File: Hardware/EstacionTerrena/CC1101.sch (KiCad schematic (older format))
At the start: 1 part, among them U3 CC1101

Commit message: Esquema de estación terrena casi terminado. falta revision.
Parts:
- added C10, C9: 15pF, symbol Device:C_Small
- added C11, C12, C13, C14, C6, C7, C8: 100nF, symbol Device:C_Small
- added C15, C16: n.a, symbol Device:C_Small
- added L1: 12nH, symbol Device:L
- added R4: 56k, symbol Device:R
- added R5, R6: 0R, symbol Device:R
- added U5: 0915BM15A0001, symbol AXTEC_IC:0915BM15A0001
- added Y2: 26MHz, symbol Device:Crystal_GND2
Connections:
- net labels added: RF_N, RF_P
- wire segments 20 -> 80

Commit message: Asignados footprints a esquema de estación terrena
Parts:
- removed U5: 0915BM15A0001, symbol AXTEC_IC:0915BM15A0001
- removed Y2: 26MHz, symbol Device:Crystal_GND2
- added U5: 0915BM15A0001E, 0915BM15A0001E, symbol SamacSys_Parts:0915BM15A0001E
- added Y2: 26 MHz, Crystal:Crystal_SMD_2520-4Pin_2.5x2.0mm, symbol Device:Crystal_GND24
- C10, C9: value 15pF -> 18pF; footprint (none) -> Capacitor_SMD:C_0603_1608Metric; Dielectric (none) -> NP0; Manufacturer Part Number (none) -> VJ0603A180KXQPW1BC; Voltage (none) -> 10V
- C11, C12, C13, C14, C6, C7, C8: footprint (none) -> Capacitor_SMD:C_0603_1608Metric; Dielectric (none) -> X7R; Manufacturer Part Number (none) -> EMK107B7104KAHT; Voltage (none) -> 16V
- C15, C16: footprint (none) -> Capacitor_SMD:C_0402_1005Metric
- L1: footprint (none) -> Inductor_SMD:L_0402_1005Metric; Manufacturer Part Number (none) -> L-07C12NJV6
- R5, R6: footprint (none) -> Resistor_SMD:R_0402_1005Metric; Manufacturer Part Number (none) -> RC0402JR-070RL
- renumbered U3 to U4
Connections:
- wire segments 80 -> 79
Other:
- moved on the sheet: C15, C16, L1, R5

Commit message: PCB inicial para estación terrena
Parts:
- removed U4: CC1101, symbol AXTEC_IC:CC1101
- added U4: CC1101RGP, QFN50P400X400X100-21N-D, symbol SamacSys_Parts:CC1101RGP
- R4: footprint (none) -> Resistor_SMD:R_0603_1608Metric_Pad1.05x0.95mm_HandSolder
- renumbered C13 to C12, C12 to C13
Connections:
- wire segments 79 -> 80
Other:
- moved on the sheet: C10, C11, C12, C13, C14, C15, C16, C6, C7, C8, C9, L1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

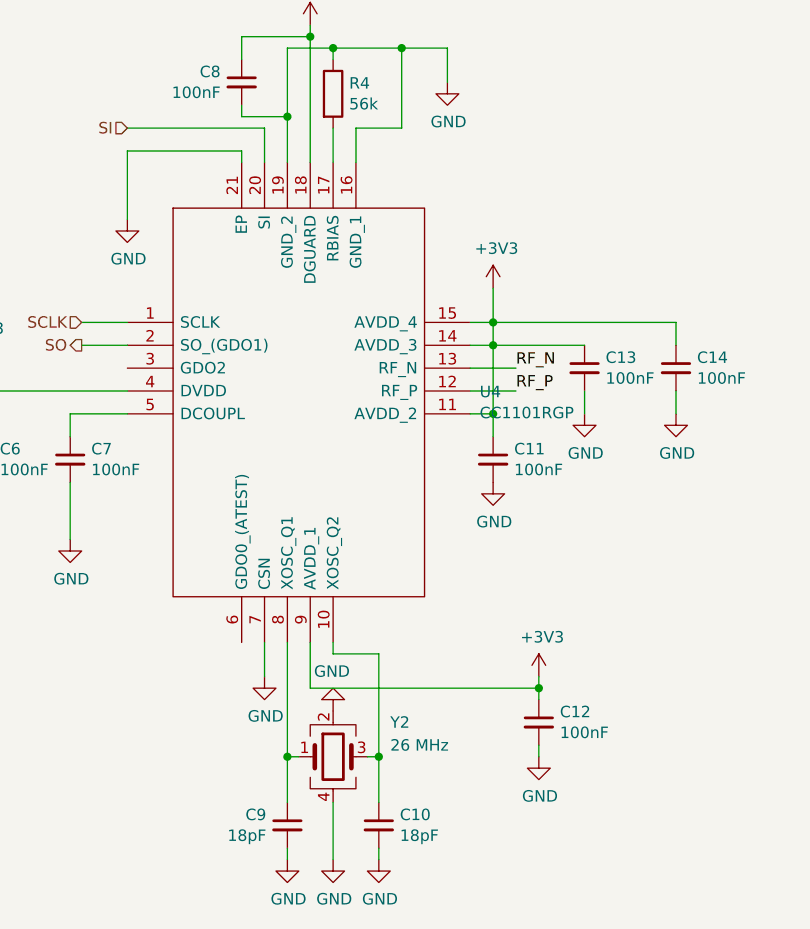
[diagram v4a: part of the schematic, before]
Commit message: Numeros de parte para estación terrena. Capacitores de 15pF para cristal de CC1101 (en lugar de 18pF).
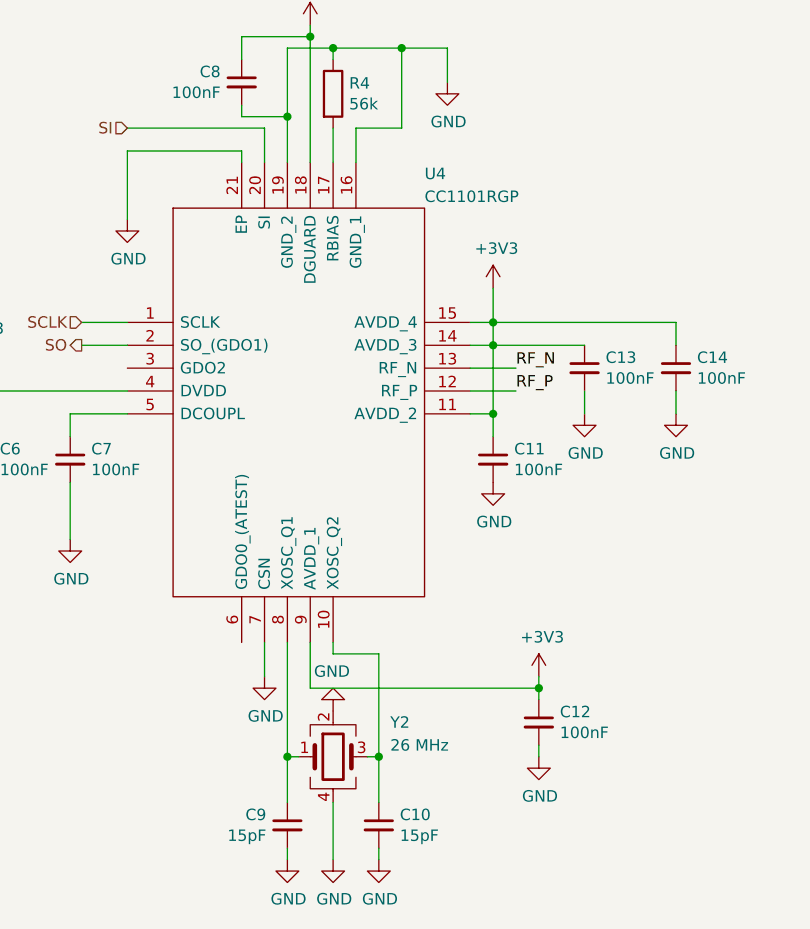
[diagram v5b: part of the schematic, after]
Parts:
- C10, C9: value 18pF -> 15pF; Manufacturer Part Number VJ0603A180KXQPW1BC -> VJ0603A150KXJPW1BC
- R4: Manufacturer Part Number (none) -> RC0402FR-0756KL
- U4: Manufacturer Part Number (none) -> CC1101RGP; Manufacturer_Part_Number CC1101RGP -> (none)
- U5: Manufacturer Part Number (none) -> 0915BM15A0001E; Manufacturer_Part_Number 0915BM15A0001E -> (none)
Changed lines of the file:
@@
 F 2 "Resistor_SMD:R_0603_1608Metric_Pad1.05x0.95mm_HandSolder" V 3730 2150 50  0001 C CNN
 F 3 "~" H 3800 2150 50  0001 C CNN
+F 4 "RC0402FR-0756KL" H 3800 2150 50  0001 C CNN "Manufacturer Part Number"
 	1    3800 2150
 	1    0    0    -1
@@
 AR Path="/5B9A8077/5BF04031" Ref="C9"  Part="1"
 F 0 "C9" H 3692 5396 50  0000 L CNN
-F 1 "18pF" H 3692 5305 50  0000 L CNN
+F 1 "15pF" H 3692 5305 50  0000 L CNN
 F 2 "Capacitor_SMD:C_0603_1608Metric" H 3600 5350 50  0001 C CNN
 F 3 "~" H 3600 5350 50  0001 C CNN
 F 4 "NP0" H 3600 5350 50  0001 C CNN "Dielectric"
 F 5 "10V" H 3600 5350 50  0001 C CNN "Voltage"
-F 6 "VJ0603A180KXQPW1BC" H 3600 5350 50  0001 C CNN "Manufacturer Part Number"
+F 6 "VJ0603A150KXJPW1BC" H 3600 5350 50  0001 C CNN "Manufacturer Part Number"
 	1    3600 5350
 	-1   0    0    -1
@@
 AR Path="/5B9A8077/5BF0725F" Ref="C10"  Part="1"
 F 0 "C10" H 4092 5396 50  0000 L CNN
-F 1 "18pF" H 4092 5305 50  0000 L CNN
+F 1 "15pF" H 4092 5305 50  0000 L CNN
 F 2 "Capacitor_SMD:C_0603_1608Metric" H 4000 5350 50  0001 C CNN
 F 3 "~" H 4000 5350 50  0001 C CNN
 F 4 "NP0" H 4000 5350 50  0001 C CNN "Dielectric"
 F 5 "10V" H 4000 5350 50  0001 C CNN "Voltage"
-F 6 "VJ0603A180KXQPW1BC" H 4000 5350 50  0001 C CNN "Manufacturer Part Number"
+F 6 "VJ0603A150KXJPW1BC" H 4000 5350 50  0001 C CNN "Manufacturer Part Number"
 	1    4000 5350
 	1    0    0    -1
@@
 F 5 "0.8" H 7500 3300 50  0001 L CNN "Height"
 F 6 "JOHANSON TECHNOLOGY" H 7500 3200 50  0001 L CNN "Manufacturer_Name"
-F 7 "0915BM15A0001E" H 7500 3100 50  0001 L CNN "Manufacturer_Part_Number"
+F 7 "0915BM15A0001E" H 7500 3100 50  0001 L CNN "Manufacturer Part Number"
 F 8 "0915BM15A0001E" H 7500 3000 50  0001 L CNN "Arrow Part Number"
 	1    7150 3400
@@
 U 1 1 5BBFFFB0
 P 2900 3150
-F 0 "U4" H 4441 2846 50  0000 L CNN
-F 1 "CC1101RGP" H 4441 2754 50  0000 L CNN
+F 0 "U4" H 4200 3800 50  0000 L CNN
+F 1 "CC1101RGP" H 4200 3700 50  0000 L CNN
 F 2 "QFN50P400X400X100-21N-D" H 4250 3650 50  0001 L CNN
 F 3 "http://www.ti.com/lit/ds/symlink/cc1101.pdf" H 4250 3550 50  0001 L CNN
@@
 F 5 "1" H 4250 3350 50  0001 L CNN "Height"
 F 6 "Texas Instruments" H 4250 3250 50  0001 L CNN "Manufacturer_Name"
-F 7 "CC1101RGP" H 4250 3150 50  0001 L CNN "Manufacturer_Part_Number"
+F 7 "CC1101RGP" H 4250 3150 50  0001 L CNN "Manufacturer Part Number"
 F 8 "8203068P" H 4250 3050 50  0001 L CNN "RS Part Number"
 F 9 "http://uk.rs-online.com/web/p/products/8203068P" H 4250 2950 50  0001 L CNN "RS Price/Stock"

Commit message: Agregado jumper para CS en estacion terrena
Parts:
- U4: footprint QFN50P400X400X100-21N-D -> SamacSys_Parts:QFN50P400X400X100-21N-D
- U5: footprint 0915BM15A0001E -> SamacSys_Parts:0915BM15A0001E
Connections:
- net GND: no longer U4.7 (CSN)
- new net CS: U4.7 (CSN)
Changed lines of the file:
@@
 Text HLabel 2900 2300 0    50   Input ~ 0
 SI
-$Comp
-L power:GND #PWR026
-U 1 1 5B9A819D
-P 3500 4700
-F 0 "#PWR026" H 3500 4450 50  0001 C CNN
-F 1 "GND" H 3505 4527 50  0000 C CNN
-F 2 "" H 3500 4700 50  0001 C CNN
-F 3 "" H 3500 4700 50  0001 C CNN
-	1    3500 4700
-	1    0    0    -1
-$EndComp
-Wire Wire Line
-	3500 4700 3500 4550
 Text HLabel 9400 3500 2    50   BiDi ~ 0
 ANT
@@
 F 0 "U5" H 7150 3766 50  0000 C CNN
 F 1 "0915BM15A0001E" H 7150 3674 50  0000 C CNN
-F 2 "0915BM15A0001E" H 7500 3600 50  0001 L CNN
+F 2 "SamacSys_Parts:0915BM15A0001E" H 7500 3600 50  0001 L CNN
 F 3 "http://www.mouser.com/datasheet/2/611/0915BM15A0001-242333.pdf" H 7500 3500 50  0001 L CNN
 F 4 "Signal Conditioning 915MHz BALUN/FILTER" H 7500 3400 50  0001 L CNN "Description"
@@
 F 0 "U4" H 4200 3800 50  0000 L CNN
 F 1 "CC1101RGP" H 4200 3700 50  0000 L CNN
-F 2 "QFN50P400X400X100-21N-D" H 4250 3650 50  0001 L CNN
+F 2 "SamacSys_Parts:QFN50P400X400X100-21N-D" H 4250 3650 50  0001 L CNN
 F 3 "http://www.ti.com/lit/ds/symlink/cc1101.pdf" H 4250 3550 50  0001 L CNN
 F 4 "Texas Instruments CC1101RGP, RF Transceiver IC Triple Band 1.8  3.6 V 20-Pin QFN" H 4250 3450 50  0001 L CNN "Description"
@@
 	1    0    0    -1
 $EndComp
+Text HLabel 3150 4700 0    50   Input ~ 0
+CS
+Wire Wire Line
+	3150 4700 3500 4700
+Wire Wire Line
+	3500 4700 3500 4550
 $EndSCHEMATC

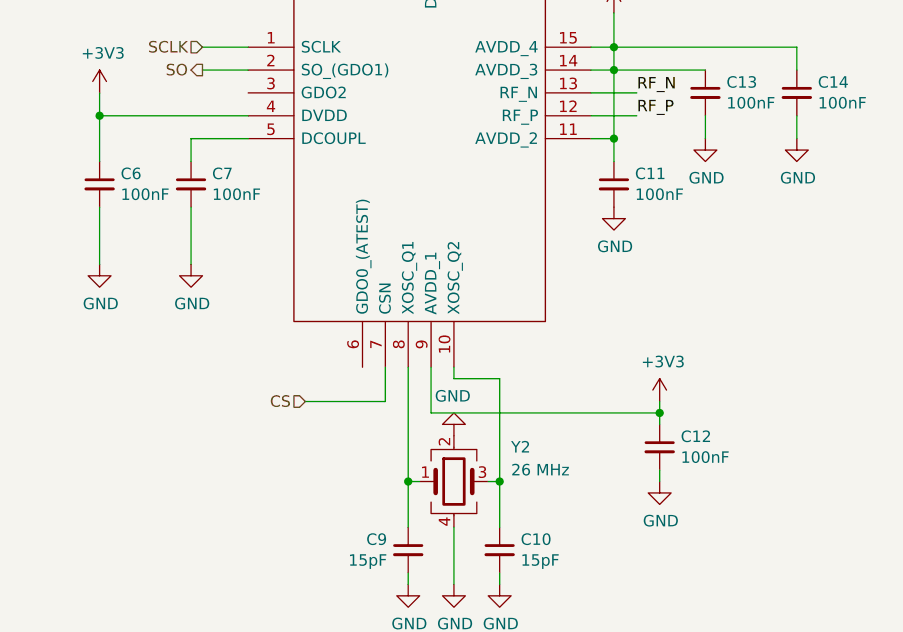
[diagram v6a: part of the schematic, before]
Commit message: Componentes 0402 para el CC1101 en estación terrena
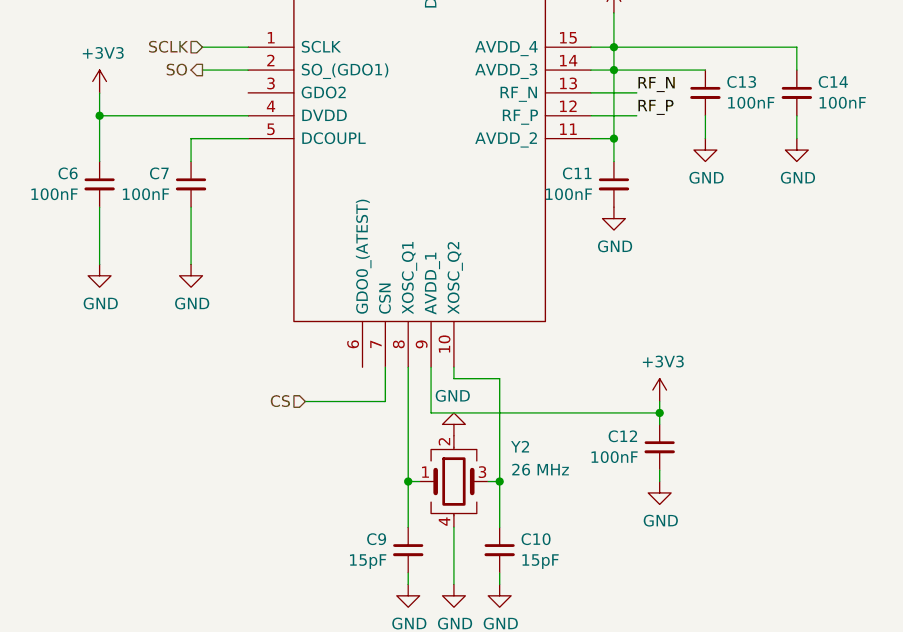
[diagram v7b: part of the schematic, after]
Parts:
- C10, C9: footprint Capacitor_SMD:C_0603_1608Metric -> Capacitor_SMD:C_0402_1005Metric; Manufacturer Part Number VJ0603A150KXJPW1BC -> C0402C150J5GACTU
- C11, C12, C13, C14, C6, C7, C8: footprint Capacitor_SMD:C_0603_1608Metric -> Capacitor_SMD:C_0402_1005Metric; Manufacturer Part Number EMK107B7104KAHT -> GCM155R71C104KA55D
- R4: footprint Resistor_SMD:R_0603_1608Metric_Pad1.05x0.95mm_HandSolder -> Resistor_SMD:R_0402_1005Metric
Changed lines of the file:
@@
 F 0 "R4" H 3870 2196 50  0000 L CNN
 F 1 "56k" H 3870 2105 50  0000 L CNN
-F 2 "Resistor_SMD:R_0603_1608Metric_Pad1.05x0.95mm_HandSolder" V 3730 2150 50  0001 C CNN
+F 2 "Resistor_SMD:R_0402_1005Metric" V 3730 2150 50  0001 C CNN
 F 3 "~" H 3800 2150 50  0001 C CNN
 F 4 "RC0402FR-0756KL" H 3800 2150 50  0001 C CNN "Manufacturer Part Number"
@@
 F 0 "C8" H 3492 2146 50  0000 L CNN
 F 1 "100nF" H 3492 2055 50  0000 L CNN
-F 2 "Capacitor_SMD:C_0603_1608Metric" H 3400 2100 50  0001 C CNN
+F 2 "Capacitor_SMD:C_0402_1005Metric" H 3400 2100 50  0001 C CNN
 F 3 "~" H 3400 2100 50  0001 C CNN
 F 4 "X7R" H 3400 2100 50  0001 C CNN "Dielectric"
 F 5 "16V" H 3400 2100 50  0001 C CNN "Voltage"
-F 6 "EMK107B7104KAHT" H 3400 2100 50  0001 C CNN "Manufacturer Part Number"
+F 6 "GCM155R71C104KA55D" H 3400 2100 50  0001 C CNN "Manufacturer Part Number"
 	1    3400 2100
 	-1   0    0    -1
-$EndComp
-$Comp
-L Device:C_Small C?
-U 1 1 5BEFB6E8
-P 2250 3750
-AR Path="/5B9997DB/5BEFB6E8" Ref="C?"  Part="1"
-AR Path="/5B9A8077/5BEFB6E8" Ref="C6"  Part="1"
-F 0 "C6" H 2342 3796 50  0000 L CNN
-F 1 "100nF" H 2342 3705 50  0000 L CNN
-F 2 "Capacitor_SMD:C_0603_1608Metric" H 2250 3750 50  0001 C CNN
-F 3 "~" H 2250 3750 50  0001 C CNN
-F 4 "X7R" H 2250 3750 50  0001 C CNN "Dielectric"
-F 5 "16V" H 2250 3750 50  0001 C CNN "Voltage"
-F 6 "EMK107B7104KAHT" H 2250 3750 50  0001 C CNN "Manufacturer Part Number"
-	1    2250 3750
-	1    0    0    -1
-$EndComp
-$Comp
-L Device:C_Small C?
-U 1 1 5BEFB74F
-P 2650 3750
-AR Path="/5B9997DB/5BEFB74F" Ref="C?"  Part="1"
-AR Path="/5B9A8077/5BEFB74F" Ref="C7"  Part="1"
-F 0 "C7" H 2742 3796 50  0000 L CNN
-F 1 "100nF" H 2742 3705 50  0000 L CNN
-F 2 "Capacitor_SMD:C_0603_1608Metric" H 2650 3750 50  0001 C CNN
-F 3 "~" H 2650 3750 50  0001 C CNN
-F 4 "X7R" H 2650 3750 50  0001 C CNN "Dielectric"
-F 5 "16V" H 2650 3750 50  0001 C CNN "Voltage"
-F 6 "EMK107B7104KAHT" H 2650 3750 50  0001 C CNN "Manufacturer Part Number"
-	1    2650 3750
-	1    0    0    -1
-$EndComp
-$Comp
-L Device:C_Small C?
-U 1 1 5BEFB898
-P 4700 4900
-AR Path="/5B9997DB/5BEFB898" Ref="C?"  Part="1"
-AR Path="/5B9A8077/5BEFB898" Ref="C12"  Part="1"
-F 0 "C12" H 4792 4946 50  0000 L CNN
-F 1 "100nF" H 4792 4855 50  0000 L CNN
-F 2 "Capacitor_SMD:C_0603_1608Metric" H 4700 4900 50  0001 C CNN
-F 3 "~" H 4700 4900 50  0001 C CNN
-F 4 "X7R" H 4700 4900 50  0001 C CNN "Dielectric"
-F 5 "16V" H 4700 4900 50  0001 C CNN "Voltage"
-F 6 "EMK107B7104KAHT" H 4700 4900 50  0001 C CNN "Manufacturer Part Number"
-	1    4700 4900
-	1    0    0    -1
-$EndComp
-$Comp
-L Device:C_Small C?
-U 1 1 5BEFBAA8
-P 4500 3750
-AR Path="/5B9997DB/5BEFBAA8" Ref="C?"  Part="1"
-AR Path="/5B9A8077/5BEFBAA8" Ref="C11"  Part="1"
-F 0 "C11" H 4592 3796 50  0000 L CNN
-F 1 "100nF" H 4592 3705 50  0000 L CNN
-F 2 "Capacitor_SMD:C_0603_1608Metric" H 4500 3750 50  0001 C CNN
-F 3 "~" H 4500 3750 50  0001 C CNN
-F 4 "X7R" H 4500 3750 50  0001 C CNN "Dielectric"
-F 5 "16V" H 4500 3750 50  0001 C CNN "Voltage"
-F 6 "EMK107B7104KAHT" H 4500 3750 50  0001 C CNN "Manufacturer Part Number"
-	1    4500 3750
-	1    0    0    -1
-$EndComp
-$Comp
-L Device:C_Small C?
-U 1 1 5BEFBAF0
-P 4900 3350
-AR Path="/5B9997DB/5BEFBAF0" Ref="C?"  Part="1"
-AR Path="/5B9A8077/5BEFBAF0" Ref="C13"  Part="1"
-F 0 "C13" H 4992 3396 50  0000 L CNN
-F 1 "100nF" H 4992 3305 50  0000 L CNN
-F 2 "Capacitor_SMD:C_0603_1608Metric" H 4900 3350 50  0001 C CNN
-F 3 "~" H 4900 3350 50  0001 C CNN
-F 4 "X7R" H 4900 3350 50  0001 C CNN "Dielectric"
-F 5 "16V" H 4900 3350 50  0001 C CNN "Voltage"
-F 6 "EMK107B7104KAHT" H 4900 3350 50  0001 C CNN "Manufacturer Part Number"
-	1    4900 3350
-	1    0    0    -1
-$EndComp
-$Comp
-L Device:C_Small C?
-U 1 1 5BEFBB3E
-P 5300 3350
-AR Path="/5B9997DB/5BEFBB3E" Ref="C?"  Part="1"
-AR Path="/5B9A8077/5BEFBB3E" Ref="C14"  Part="1"
-F 0 "C14" H 5392 3396 50  0000 L CNN
-F 1 "100nF" H 5392 3305 50  0000 L CNN
-F 2 "Capacitor_SMD:C_0603_1608Metric" H 5300 3350 50  0001 C CNN
-F 3 "~" H 5300 3350 50  0001 C CNN
-F 4 "X7R" H 5300 3350 50  0001 C CNN "Dielectric"
-F 5 "16V" H 5300 3350 50  0001 C CNN "Voltage"
-F 6 "EMK107B7104KAHT" H 5300 3350 50  0001 C CNN "Manufacturer Part Number"
-	1    5300 3350
-	1    0    0    -1
 $EndComp
 $Comp
@@
 F 0 "C9" H 3692 5396 50  0000 L CNN
 F 1 "15pF" H 3692 5305 50  0000 L CNN
-F 2 "Capacitor_SMD:C_0603_1608Metric" H 3600 5350 50  0001 C CNN
+F 2 "Capacitor_SMD:C_0402_1005Metric" H 3600 5350 50  0001 C CNN
 F 3 "~" H 3600 5350 50  0001 C CNN
 F 4 "NP0" H 3600 5350 50  0001 C CNN "Dielectric"
 F 5 "10V" H 3600 5350 50  0001 C CNN "Voltage"
-F 6 "VJ0603A150KXJPW1BC" H 3600 5350 50  0001 C CNN "Manufacturer Part Number"
+F 6 "C0402C150J5GACTU" H 3600 5350 50  0001 C CNN "Manufacturer Part Number"
 	1    3600 5350
 	-1   0    0    -1
-$EndComp
-$Comp
-L Device:C_Small C?
-U 1 1 5BF0725F
-P 4000 5350
-AR Path="/5B9997DB/5BF0725F" Ref="C?"  Part="1"
-AR Path="/5B9A8077/5BF0725F" Ref="C10"  Part="1"
-F 0 "C10" H 4092 5396 50  0000 L CNN
-F 1 "15pF" H 4092 5305 50  0000 L CNN
-F 2 "Capacitor_SMD:C_0603_1608Metric" H 4000 5350 50  0001 C CNN
-F 3 "~" H 4000 5350 50  0001 C CNN
-F 4 "NP0" H 4000 5350 50  0001 C CNN "Dielectric"
-F 5 "10V" H 4000 5350 50  0001 C CNN "Voltage"
-F 6 "VJ0603A150KXJPW1BC" H 4000 5350 50  0001 C CNN "Manufacturer Part Number"
-	1    4000 5350
-	1    0    0    -1
 $EndComp
 $Comp
@@
 Wire Wire Line
 	3500 4700 3500 4550
+$Comp
+L Device:C_Small C?
+U 1 1 5C01AB4E
+P 2250 3750
+AR Path="/5B9997DB/5C01AB4E" Ref="C?"  Part="1"
+AR Path="/5B9A8077/5C01AB4E" Ref="C6"  Part="1"
+F 0 "C6" H 2342 3796 50  0000 L CNN
+F 1 "100nF" H 2342 3705 50  0000 L CNN
+F 2 "Capacitor_SMD:C_0402_1005Metric" H 2250 3750 50  0001 C CNN
+F 3 "~" H 2250 3750 50  0001 C CNN
+F 4 "X7R" H 2250 3750 50  0001 C CNN "Dielectric"
+F 5 "16V" H 2250 3750 50  0001 C CNN "Voltage"
+F 6 "GCM155R71C104KA55D" H 2250 3750 50  0001 C CNN "Manufacturer Part Number"
+	1    2250 3750
+	-1   0    0    -1
+$EndComp
+$Comp
+L Device:C_Small C?
+U 1 1 5C01AD13
+P 2650 3750
+AR Path="/5B9997DB/5C01AD13" Ref="C?"  Part="1"
+AR Path="/5B9A8077/5C01AD13" Ref="C7"  Part="1"
+F 0 "C7" H 2742 3796 50  0000 L CNN
+F 1 "100nF" H 2742 3705 50  0000 L CNN
+F 2 "Capacitor_SMD:C_0402_1005Metric" H 2650 3750 50  0001 C CNN
+F 3 "~" H 2650 3750 50  0001 C CNN
+F 4 "X7R" H 2650 3750 50  0001 C CNN "Dielectric"
+F 5 "16V" H 2650 3750 50  0001 C CNN "Voltage"
+F 6 "GCM155R71C104KA55D" H 2650 3750 50  0001 C CNN "Manufacturer Part Number"
+	1    2650 3750
+	-1   0    0    -1
+$EndComp
+$Comp
+L Device:C_Small C?
+U 1 1 5C01B2C0
+P 4700 4900
+AR Path="/5B9997DB/5C01B2C0" Ref="C?"  Part="1"
+AR Path="/5B9A8077/5C01B2C0" Ref="C12"  Part="1"
+F 0 "C12" H 4792 4946 50  0000 L CNN
+F 1 "100nF" H 4792 4855 50  0000 L CNN
+F 2 "Capacitor_SMD:C_0402_1005Metric" H 4700 4900 50  0001 C CNN
+F 3 "~" H 4700 4900 50  0001 C CNN
+F 4 "X7R" H 4700 4900 50  0001 C CNN "Dielectric"
+F 5 "16V" H 4700 4900 50  0001 C CNN "Voltage"
+F 6 "GCM155R71C104KA55D" H 4700 4900 50  0001 C CNN "Manufacturer Part Number"
+	1    4700 4900
+	-1   0    0    -1
+$EndComp
+$Comp
+L Device:C_Small C?
+U 1 1 5C01B4BF
+P 4500 3750
+AR Path="/5B9997DB/5C01B4BF" Ref="C?"  Part="1"
+AR Path="/5B9A8077/5C01B4BF" Ref="C11"  Part="1"
+F 0 "C11" H 4592 3796 50  0000 L CNN
+F 1 "100nF" H 4592 3705 50  0000 L CNN
+F 2 "Capacitor_SMD:C_0402_1005Metric" H 4500 3750 50  0001 C CNN
+F 3 "~" H 4500 3750 50  0001 C CNN
+F 4 "X7R" H 4500 3750 50  0001 C CNN "Dielectric"
+F 5 "16V" H 4500 3750 50  0001 C CNN "Voltage"
+F 6 "GCM155R71C104KA55D" H 4500 3750 50  0001 C CNN "Manufacturer Part Number"
+	1    4500 3750
+	-1   0    0    -1
+$EndComp
+$Comp
+L Device:C_Small C?
+U 1 1 5C020579
+P 4900 3350
+AR Path="/5B9997DB/5C020579" Ref="C?"  Part="1"
+AR Path="/5B9A8077/5C020579" Ref="C13"  Part="1"
+F 0 "C13" H 4992 3396 50  0000 L CNN
+F 1 "100nF" H 4992 3305 50  0000 L CNN
+F 2 "Capacitor_SMD:C_0402_1005Metric" H 4900 3350 50  0001 C CNN
+F 3 "~" H 4900 3350 50  0001 C CNN
+F 4 "X7R" H 4900 3350 50  0001 C CNN "Dielectric"
+F 5 "16V" H 4900 3350 50  0001 C CNN "Voltage"
+F 6 "GCM155R71C104KA55D" H 4900 3350 50  0001 C CNN "Manufacturer Part Number"
+	1    4900 3350
+	1    0    0    -1
+$EndComp
+$Comp
+L Device:C_Small C?
+U 1 1 5C02209B
+P 5300 3350
+AR Path="/5B9997DB/5C02209B" Ref="C?"  Part="1"
+AR Path="/5B9A8077/5C02209B" Ref="C14"  Part="1"
+F 0 "C14" H 5392 3396 50  0000 L CNN
+F 1 "100nF" H 5392 3305 50  0000 L CNN
+F 2 "Capacitor_SMD:C_0402_1005Metric" H 5300 3350 50  0001 C CNN
+F 3 "~" H 5300 3350 50  0001 C CNN
+F 4 "X7R" H 5300 3350 50  0001 C CNN "Dielectric"
+F 5 "16V" H 5300 3350 50  0001 C CNN "Voltage"
+F 6 "GCM155R71C104KA55D" H 5300 3350 50  0001 C CNN "Manufacturer Part Number"
+	1    5300 3350
+	1    0    0    -1
+$EndComp
+$Comp
+L Device:C_Small C?
+U 1 1 5C0231C6
+P 4000 5350
+AR Path="/5B9997DB/5C0231C6" Ref="C?"  Part="1"
+AR Path="/5B9A8077/5C0231C6" Ref="C10"  Part="1"
+F 0 "C10" H 4092 5396 50  0000 L CNN
+F 1 "15pF" H 4092 5305 50  0000 L CNN
+F 2 "Capacitor_SMD:C_0402_1005Metric" H 4000 5350 50  0001 C CNN
+F 3 "~" H 4000 5350 50  0001 C CNN
+F 4 "NP0" H 4000 5350 50  0001 C CNN "Dielectric"
+F 5 "10V" H 4000 5350 50  0001 C CNN "Voltage"
+F 6 "C0402C150J5GACTU" H 4000 5350 50  0001 C CNN "Manufacturer Part Number"
+	1    4000 5350
+	1    0    0    -1
+$EndComp
 $EndSCHEMATC
